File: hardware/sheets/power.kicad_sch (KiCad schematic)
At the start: 19 parts, among them J1 USB_C_Receptacle, U1 CH224K, U2 TPS563200

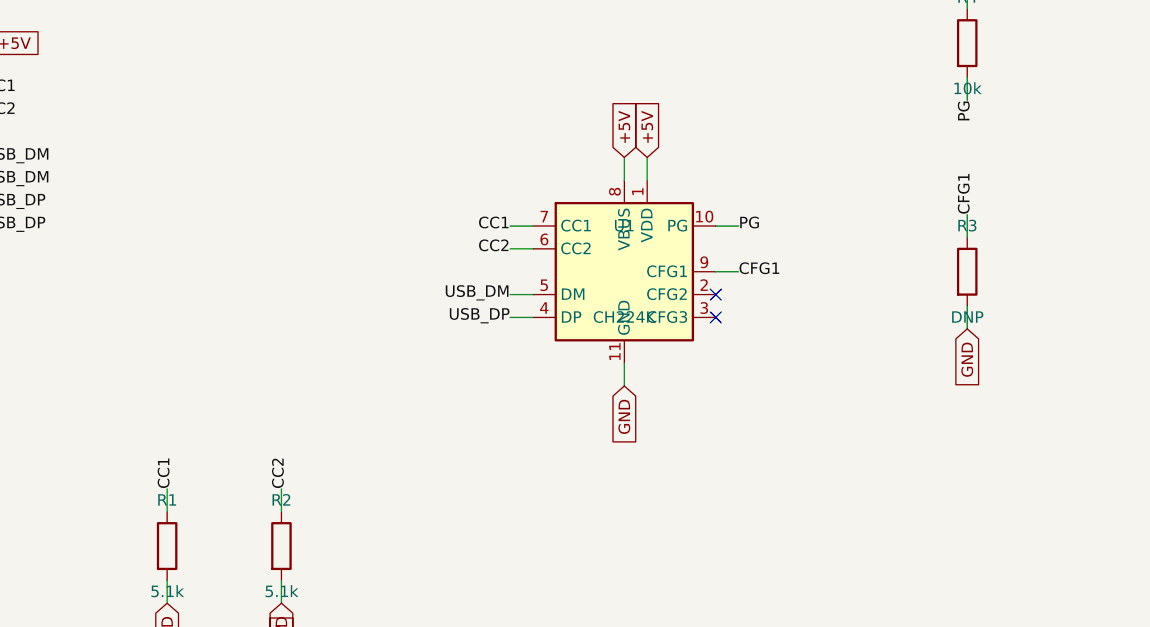
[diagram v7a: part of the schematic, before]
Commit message: Fix all critical+high design-review findings (C1-C5, H1-H8)
Full review in hardware/notes/design-review-2026-07-03.md (with per-item
fix logs). Highlights:
- SRAM strobed by gated MEMR/MEMW (was raw ~RD/~WR: I/O cycles corrupted
  SRAM and the boot shadow-load could never write it)
- Reset chain implemented: NAND combine of ~PWRGOOD + ~CPURESET drives
  V20 RESET and an always-driven RESET_DRV (dropped from the Bus MCU)
- Contention-free bus handoff: '573 OE=HLDA vs counter '244 stage
  ~OE=~HLDA; strobe gates wired + tri-stated ('125, ~OE=HLDA); Bus MCU
  address group fixed to sense; AEN/TC fixed drive; BALE input-only
- '573 LE driven by BALE (was a dangling BALE_L label)
- Data '245 DIR=DT/~R, ~OE=DEN so INTA vectors reach the CPU
- Idle pulls: strobes/DEN high, AEN/IRQ2-9/DRQ low, IOCHRDY/IOCHCK/
  DACK2-3 high
- CH224K CFG1 left open (grounding it selects 9-20V, not 5V)
- XT-IDE INTRQ pull-down (pull-up parked IRQ5 asserted)
- LPT status bit7 = ~Busy via spare inverter (SPP semantics)
- Audio summer TL072 -> MCP6002 (RRIO; TL072 out of spec at +5V single
  supply)
- card_isatest: DUT P-FET gate to V5RAW + NPN driver (default off, can
  fully turn off); /3 divider TC->~PE reload actually wired

Overturned picks corrected in notes/questions-*.md. All sheets + cards
rebuilt; structural ERC = 0; fixes netlist-verified.

Co-Authored-By: Claude Fable 5 <noreply@anthropic.com>
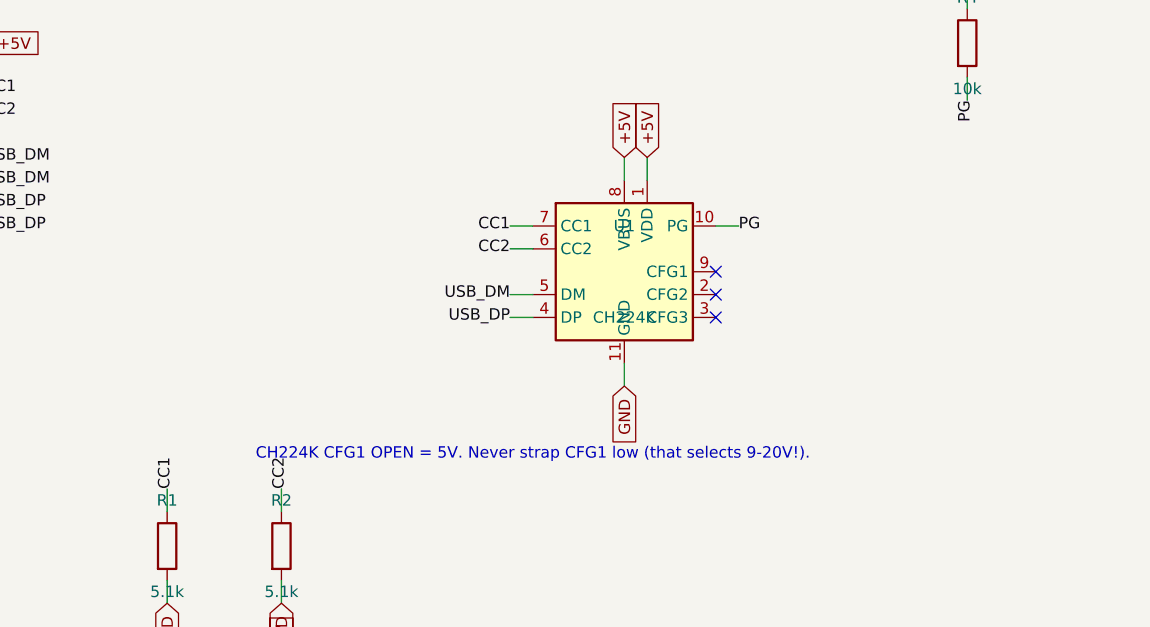
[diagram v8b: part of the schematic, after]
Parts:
- removed R3: DNP, symbol Device:R
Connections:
- net CFG1: no longer names the net of U1.9 (CFG1)
- no-connect marks 12 -> 13
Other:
- note added: "CH224K CFG1 OPEN = 5V. Never strap CFG1 low (that selects 9-20V!)."
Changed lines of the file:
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@@
 		)
 	)
-	(wire
-		(pts
-			(xy 149.86 165.1)
-			(xy 152.4 165.1)
-		)
-		(stroke
-			(width 0)
-			(type default)
-		)
-	)
-	(label "CFG1"
-		(at 152.4 165.1 0)
-		(effects
-			(font
-				(size 1.27 1.27)
-			)
-		)
+	(no_connect
+		(at 149.86 165.1)
 	)
 	(no_connect
@@
 		(at 149.86 170.18)
 	)
-	(wire
-		(pts
-			(xy 177.8 161.29)
-			(xy 177.8 158.75)
-		)
-		(stroke
-			(width 0)
-			(type default)
-		)
-	)
-	(label "CFG1"
-		(at 177.8 158.75 90)
-		(effects
-			(font
-				(size 1.27 1.27)
-			)
-		)
-	)
-	(wire
-		(pts
-			(xy 177.8 168.91)
-			(xy 177.8 171.45)
-		)
-		(stroke
-			(width 0)
-			(type default)
-		)
-	)
-	(global_label "GND"
-		(shape input)
-		(at 177.8 171.45 270)
+	(text "CH224K CFG1 OPEN = 5V. Never strap CFG1 low (that selects 9-20V!)."
+		(at 129.54 185.42 0)
 		(effects
 			(font
@@
 		(instances
 			(project "mini-xt"
-				(path "/2e7dce83-09b2-4f89-bc6c-16aeb48854d6/7b26cc48-c18e-4076-aac1-cb67976c179b"
+				(path "/ccbe75bb-9744-49b2-888c-84927206f4cb/a4da02ef-454f-4dbd-a4ef-6a5853f742a3"
 					(reference "J901")
 					(unit 1)
@@
 		(instances
 			(project "mini-xt"
-				(path "/2e7dce83-09b2-4f89-bc6c-16aeb48854d6/7b26cc48-c18e-4076-aac1-cb67976c179b"
+				(path "/ccbe75bb-9744-49b2-888c-84927206f4cb/a4da02ef-454f-4dbd-a4ef-6a5853f742a3"
 					(reference "R901")
 					(unit 1)
@@
 		(instances
 			(project "mini-xt"
-				(path "/2e7dce83-09b2-4f89-bc6c-16aeb48854d6/7b26cc48-c18e-4076-aac1-cb67976c179b"
+				(path "/ccbe75bb-9744-49b2-888c-84927206f4cb/a4da02ef-454f-4dbd-a4ef-6a5853f742a3"
 					(reference "R902")
 					(unit 1)
@@
 		(instances
 			(project "mini-xt"
-				(path "/2e7dce83-09b2-4f89-bc6c-16aeb48854d6/7b26cc48-c18e-4076-aac1-cb67976c179b"
+				(path "/ccbe75bb-9744-49b2-888c-84927206f4cb/a4da02ef-454f-4dbd-a4ef-6a5853f742a3"
 					(reference "U901")
-					(unit 1)
-				)
-			)
-		)
-	)
-	(symbol
-		(lib_id "Device:R")
-		(at 177.8 165.1 0)
-		(unit 1)
-		(exclude_from_sim no)
-		(in_bom yes)
-		(on_board yes)
-		(dnp no)
-		(fields_autoplaced yes)
-		(property "Reference" "R3"
-			(at 177.8 160.02 0)
-			(effects
-				(font
-					(size 1.27 1.27)
-				)
-			)
-		)
-		(property "Value" "DNP"
-			(at 177.8 170.18 0)
-			(effects
-				(font
-					(size 1.27 1.27)
-				)
-			)
-		)
-		(property "Footprint" ""
-			(at 177.8 165.1 0)
-			(effects
-				(font
-					(size 1.27 1.27)
-				)
-				(hide yes)
-			)
-		)
-		(pin "1"
-		)
-		(pin "2"
-		)
-		(instances
-			(project "mini-xt"
-				(path "/2e7dce83-09b2-4f89-bc6c-16aeb48854d6/7b26cc48-c18e-4076-aac1-cb67976c179b"
-					(reference "R903")
 					(unit 1)
 				)
@@
 		(instances
 			(project "mini-xt"
-				(path "/2e7dce83-09b2-4f89-bc6c-16aeb48854d6/7b26cc48-c18e-4076-aac1-cb67976c179b"
+				(path "/ccbe75bb-9744-49b2-888c-84927206f4cb/a4da02ef-454f-4dbd-a4ef-6a5853f742a3"
 					(reference "R904")
 					(unit 1)
@@
 		(instances
 			(project "mini-xt"
-				(path "/2e7dce83-09b2-4f89-bc6c-16aeb48854d6/7b26cc48-c18e-4076-aac1-cb67976c179b"
+				(path "/ccbe75bb-9744-49b2-888c-84927206f4cb/a4da02ef-454f-4dbd-a4ef-6a5853f742a3"
 					(reference "C901")
 					(unit 1)
@@
 		(instances
 			(project "mini-xt"
-				(path "/2e7dce83-09b2-4f89-bc6c-16aeb48854d6/7b26cc48-c18e-4076-aac1-cb67976c179b"
+				(path "/ccbe75bb-9744-49b2-888c-84927206f4cb/a4da02ef-454f-4dbd-a4ef-6a5853f742a3"
 					(reference "C902")
 					(unit 1)
@@
 		(instances
 			(project "mini-xt"
-				(path "/2e7dce83-09b2-4f89-bc6c-16aeb48854d6/7b26cc48-c18e-4076-aac1-cb67976c179b"
+				(path "/ccbe75bb-9744-49b2-888c-84927206f4cb/a4da02ef-454f-4dbd-a4ef-6a5853f742a3"
 					(reference "U902")
 					(unit 1)
@@
 		(instances
 			(project "mini-xt"
-				(path "/2e7dce83-09b2-4f89-bc6c-16aeb48854d6/7b26cc48-c18e-4076-aac1-cb67976c179b"
+				(path "/ccbe75bb-9744-49b2-888c-84927206f4cb/a4da02ef-454f-4dbd-a4ef-6a5853f742a3"
 					(reference "C905")
 					(unit 1)
@@
 		(instances
 			(project "mini-xt"
-				(path "/2e7dce83-09b2-4f89-bc6c-16aeb48854d6/7b26cc48-c18e-4076-aac1-cb67976c179b"
+				(path "/ccbe75bb-9744-49b2-888c-84927206f4cb/a4da02ef-454f-4dbd-a4ef-6a5853f742a3"
 					(reference "L901")
 					(unit 1)
@@
 		(instances
 			(project "mini-xt"
-				(path "/2e7dce83-09b2-4f89-bc6c-16aeb48854d6/7b26cc48-c18e-4076-aac1-cb67976c179b"
+				(path "/ccbe75bb-9744-49b2-888c-84927206f4cb/a4da02ef-454f-4dbd-a4ef-6a5853f742a3"
 					(reference "R905")
 					(unit 1)
@@
 		(instances
 			(project "mini-xt"
-				(path "/2e7dce83-09b2-4f89-bc6c-16aeb48854d6/7b26cc48-c18e-4076-aac1-cb67976c179b"
+				(path "/ccbe75bb-9744-49b2-888c-84927206f4cb/a4da02ef-454f-4dbd-a4ef-6a5853f742a3"
 					(reference "R906")
 					(unit 1)
@@
 		(instances
 			(project "mini-xt"
-				(path "/2e7dce83-09b2-4f89-bc6c-16aeb48854d6/7b26cc48-c18e-4076-aac1-cb67976c179b"
+				(path "/ccbe75bb-9744-49b2-888c-84927206f4cb/a4da02ef-454f-4dbd-a4ef-6a5853f742a3"
 					(reference "C903")
 					(unit 1)
@@
 		(instances
 			(project "mini-xt"
-				(path "/2e7dce83-09b2-4f89-bc6c-16aeb48854d6/7b26cc48-c18e-4076-aac1-cb67976c179b"
+				(path "/ccbe75bb-9744-49b2-888c-84927206f4cb/a4da02ef-454f-4dbd-a4ef-6a5853f742a3"
 					(reference "C904")
 					(unit 1)
@@
 		(instances
 			(project "mini-xt"
-				(path "/2e7dce83-09b2-4f89-bc6c-16aeb48854d6/7b26cc48-c18e-4076-aac1-cb67976c179b"
+				(path "/ccbe75bb-9744-49b2-888c-84927206f4cb/a4da02ef-454f-4dbd-a4ef-6a5853f742a3"
 					(reference "R907")
 					(unit 1)
@@
 		(instances
 			(project "mini-xt"
-				(path "/2e7dce83-09b2-4f89-bc6c-16aeb48854d6/7b26cc48-c18e-4076-aac1-cb67976c179b"
+				(path "/ccbe75bb-9744-49b2-888c-84927206f4cb/a4da02ef-454f-4dbd-a4ef-6a5853f742a3"
 					(reference "D901")
 					(unit 1)
@@
 		(instances
 			(project "mini-xt"
-				(path "/2e7dce83-09b2-4f89-bc6c-16aeb48854d6/7b26cc48-c18e-4076-aac1-cb67976c179b"
+				(path "/ccbe75bb-9744-49b2-888c-84927206f4cb/a4da02ef-454f-4dbd-a4ef-6a5853f742a3"
 					(reference "R908")
 					(unit 1)
@@
 		(instances
 			(project "mini-xt"
-				(path "/2e7dce83-09b2-4f89-bc6c-16aeb48854d6/7b26cc48-c18e-4076-aac1-cb67976c179b"
+				(path "/ccbe75bb-9744-49b2-888c-84927206f4cb/a4da02ef-454f-4dbd-a4ef-6a5853f742a3"
 					(reference "D902")
 					(unit 1)
@@
 		(instances
 			(project "mini-xt"
-				(path "/2e7dce83-09b2-4f89-bc6c-16aeb48854d6/7b26cc48-c18e-4076-aac1-cb67976c179b"
+				(path "/ccbe75bb-9744-49b2-888c-84927206f4cb/a4da02ef-454f-4dbd-a4ef-6a5853f742a3"
 					(reference "#FLG901")
 					(unit 1)
@@
 		(instances
 			(project "mini-xt"
-				(path "/2e7dce83-09b2-4f89-bc6c-16aeb48854d6/7b26cc48-c18e-4076-aac1-cb67976c179b"
+				(path "/ccbe75bb-9744-49b2-888c-84927206f4cb/a4da02ef-454f-4dbd-a4ef-6a5853f742a3"
 					(reference "#FLG902")
 					(unit 1)
@@
 		(instances
 			(project "mini-xt"
-				(path "/2e7dce83-09b2-4f89-bc6c-16aeb48854d6/7b26cc48-c18e-4076-aac1-cb67976c179b"
+				(path "/ccbe75bb-9744-49b2-888c-84927206f4cb/a4da02ef-454f-4dbd-a4ef-6a5853f742a3"
 					(reference "#FLG903")
 					(unit 1)
@@
 		(instances
 			(project "mini-xt"
-				(path "/2e7dce83-09b2-4f89-bc6c-16aeb48854d6/7b26cc48-c18e-4076-aac1-cb67976c179b"
+				(path "/ccbe75bb-9744-49b2-888c-84927206f4cb/a4da02ef-454f-4dbd-a4ef-6a5853f742a3"
 					(reference "#PWR901")
 					(unit 1)
